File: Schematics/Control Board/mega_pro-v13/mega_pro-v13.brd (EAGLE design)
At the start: 127 x 127 mm, 65 parts, among them J1 AVR_SPI_PRG_6PTH, U1 TLC59282_DBQ_24, U4 FT232RLSSOP, Y1 RESONATORSMD

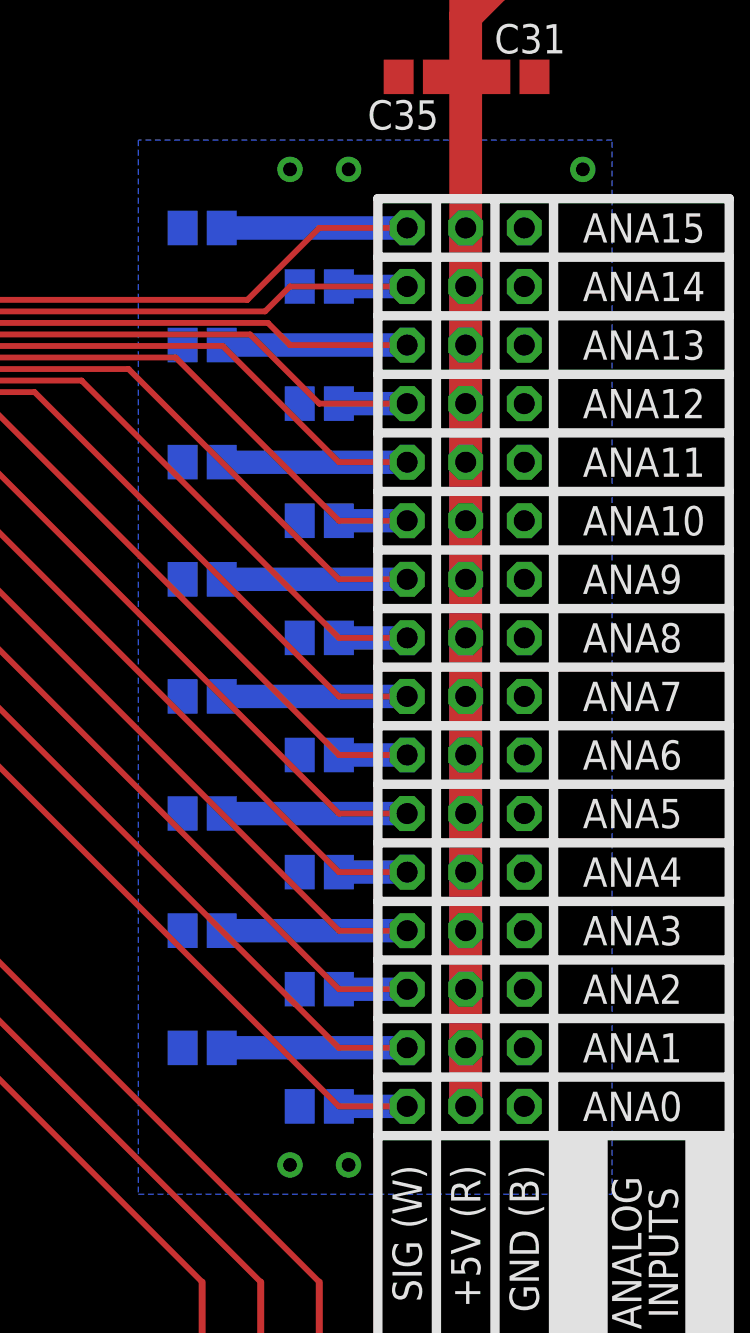
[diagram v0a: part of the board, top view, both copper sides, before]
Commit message: Updated control board schematics and board layout
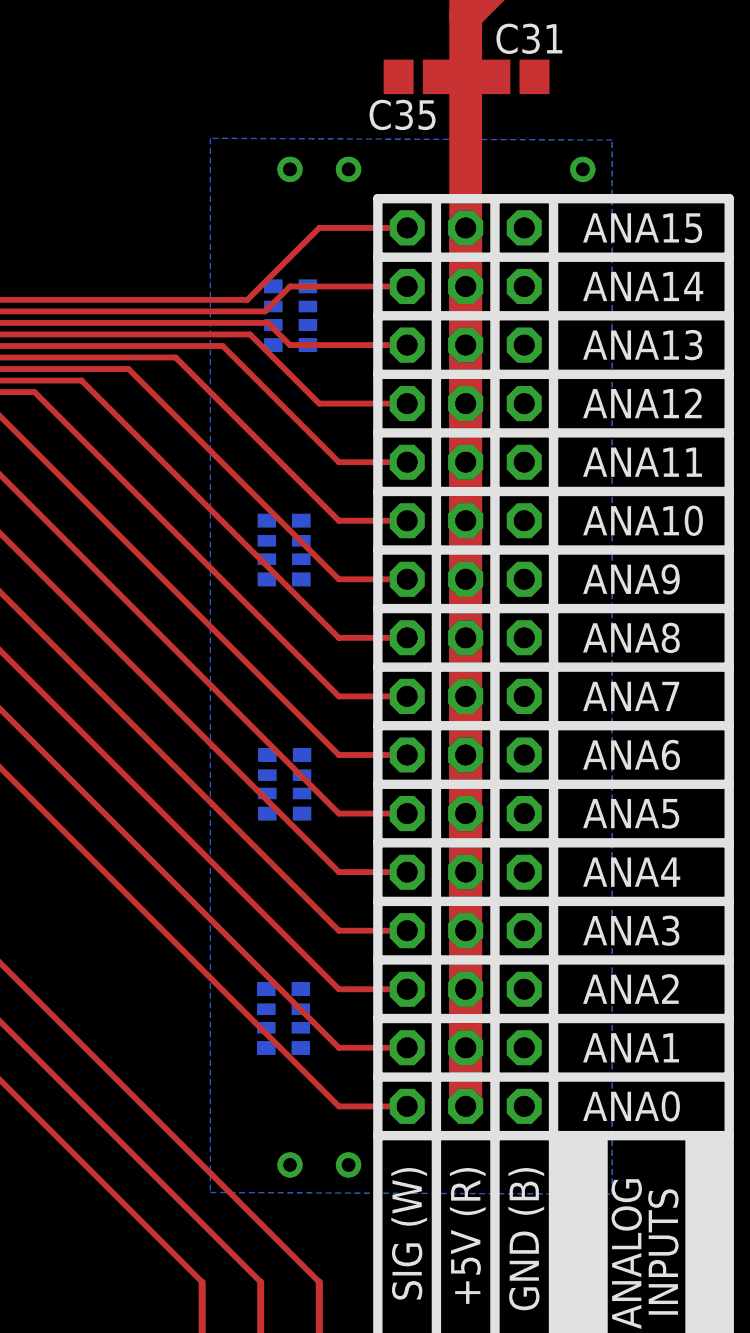
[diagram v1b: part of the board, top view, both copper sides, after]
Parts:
- removed C12, C13, C14, C15, C16, C17, C18, C19, C20, C21, C22, C23, C24, C25, C26, C27: 1uF, resistor:C0805
- added CN1, CN2, CN3, CN4: 1uF, resistor-dil:EXB38V
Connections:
- net A0: now also CN4.5; no longer C27.1
- net A1: now also CN4.6; no longer C26.1
- net A10: now also CN2.7; no longer C17.1
- net A11: now also CN2.8; no longer C16.1
- net A12: now also CN1.5; no longer C15.1
- net A13: now also CN1.6; no longer C14.1
- net A14: now also CN1.7; no longer C13.1
- net A15: now also CN1.8; no longer C12.1
- net A2: now also CN4.7; no longer C25.1
- net A3: now also CN4.8; no longer C24.1
- net A4: now also CN3.5; no longer C23.1
- net A5: now also CN3.6; no longer C22.1
- net A6: now also CN3.7; no longer C21.1
- net A7: now also CN3.8; no longer C20.1
- net A8: now also CN2.5; no longer C19.1
- net A9: now also CN2.6; no longer C18.1
- net GND: now also CN1.1, CN1.2, CN1.3, CN1.4, CN2.1, CN2.2, CN2.3, CN2.4, CN3.1, CN3.2, CN3.3, CN3.4, CN4.1, CN4.2, CN4.3, CN4.4; no longer C12.2, C13.2, C14.2, C15.2, C16.2, C17.2, C18.2, C19.2, C20.2, C21.2, C22.2, C23.2, C24.2, C25.2, C26.2, C27.2
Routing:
- net A8: track 58.8 -> 50.8 mm
- net A6: track 57.2 -> 49.1 mm
- net A4: track 55.5 -> 47.4 mm
- net A2: track 53.8 -> 45.7 mm
- net A14: track 63.9 -> 55.9 mm
- net A12: track 62.2 -> 54.2 mm
- net A10: track 60.5 -> 52.5 mm
- net A0: track 54.7 -> 46.6 mm
- net A9: track 54.6 -> 51.7 mm
- net A7: track 52.9 -> 50.0 mm
- net A5: track 51.2 -> 48.3 mm
- net A3: track 49.5 -> 46.6 mm
- net A15: track 59.7 -> 56.7 mm
- net A13: track 58.0 -> 55.0 mm
- net A11: track 56.3 -> 53.3 mm
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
